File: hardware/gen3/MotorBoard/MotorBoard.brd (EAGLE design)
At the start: 140 x 100 mm, 274 parts, among them M1O1 TEST_PT, M1O2 TEST_PT, M1O3 TEST_PT, M2O1 TEST_PT, M2O2 TEST_PT, M2O3 TEST_PT, M3O1 TEST_PT, M3O2 TEST_PT, M3O3 TEST_PT, M4O1 TEST_PT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

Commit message: resistor values for LEDs
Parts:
- R1, R101, R103, R99: value 130 -> 1k
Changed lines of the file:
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@@
 <attribute name="OC_FARNELL" value="1455104" x="108.225" y="32.425" size="1.778" layer="27" display="off"/>
 </element>
-<element name="R1" library="SparkFun-Passives" package="0805" value="130" x="73" y="91" rot="R270"/>
-<element name="R99" library="SparkFun-Passives" package="0805" value="130" x="67" y="91" rot="R270"/>
-<element name="R101" library="SparkFun-Passives" package="0805" value="130" x="79" y="91" rot="R270"/>
-<element name="R103" library="SparkFun-Passives" package="0805" value="130" x="61" y="91" rot="R270"/>
+<element name="R1" library="SparkFun-Passives" package="0805" value="1k" x="73" y="91" rot="R270"/>
+<element name="R99" library="SparkFun-Passives" package="0805" value="1k" x="67" y="91" rot="R270"/>
+<element name="R101" library="SparkFun-Passives" package="0805" value="1k" x="79" y="91" rot="R270"/>
+<element name="R103" library="SparkFun-Passives" package="0805" value="1k" x="61" y="91" rot="R270"/>
 <element name="LED9" library="SparkFun-LED" package="LED-1206" value="" x="73" y="95.7" rot="R90"/>
 <element name="LED11" library="SparkFun-LED" package="LED-1206" value="" x="67" y="95.7" rot="R90"/>

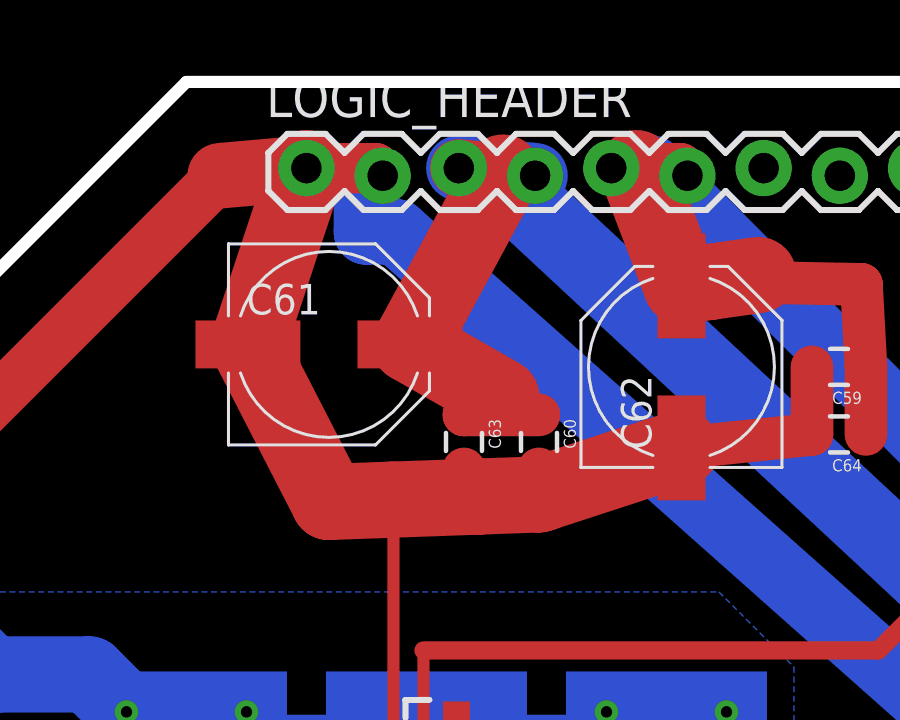
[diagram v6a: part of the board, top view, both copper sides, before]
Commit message: using more pins on logic header
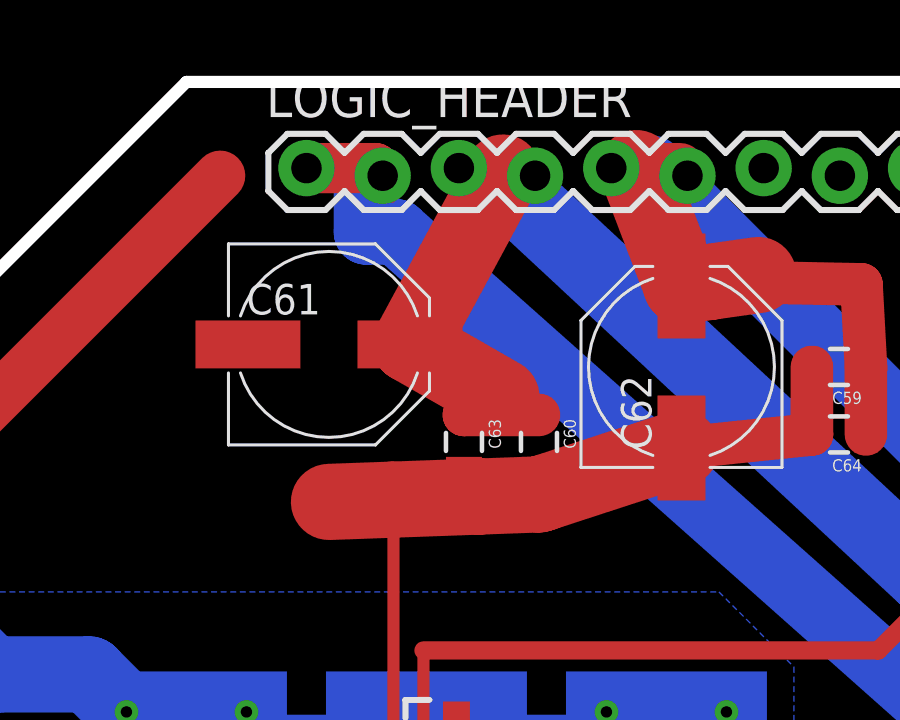
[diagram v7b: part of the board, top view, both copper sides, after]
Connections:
- net 3.3V: now also LOGIC_HEADER.5, LOGIC_HEADER.6, LOGIC_HEADER.7; no longer LOGIC_HEADER.3, LOGIC_HEADER.4
- net 5V: now also LOGIC_HEADER.10, LOGIC_HEADER.8, LOGIC_HEADER.9; no longer LOGIC_HEADER.5, LOGIC_HEADER.6
- net GND: now also LOGIC_HEADER.3, LOGIC_HEADER.4
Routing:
- net GND: track 859.3 -> 842.4 mm
- net 3.3V: track 448.1 -> 442.9 mm
- net 5V: track 654.6 -> 653.4 mm
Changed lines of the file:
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@@
 <via x="65.8" y="59" extent="1-16" drill="0.381"/>
 <via x="44.85" y="77.9" extent="1-16" drill="0.381"/>
-<contactref element="C60" pad="2"/>
-<contactref element="C61" pad="-"/>
 <contactref element="C62" pad="-"/>
 <contactref element="C59" pad="2"/>
-<contactref element="C63" pad="2"/>
 <contactref element="C64" pad="2"/>
-<contactref element="LOGIC_HEADER" pad="1"/>
-<contactref element="LOGIC_HEADER" pad="2"/>
-<wire x1="24" y1="97.127" x2="26.286" y2="97.127" width="1.6764" layer="1"/>
-<wire x1="26.286" y1="97.127" x2="26.54" y2="96.873" width="1.6764" layer="1"/>
-<wire x1="26.85" y1="96.1" x2="26.54" y2="96.873" width="0.254" layer="1"/>
 <contactref element="C46" pad="2"/>
 <contactref element="C45" pad="2"/>
@@
 <via x="89.5" y="24.75" extent="1-16" drill="0.508"/>
 <via x="89.5" y="27" extent="1-16" drill="0.508"/>
-<wire x1="21.123" y1="96.873" x2="24" y2="97.127" width="2.1844" layer="1"/>
-<wire x1="22.05" y1="91.25" x2="24" y2="97.127" width="2.54" layer="1"/>
 <wire x1="36.5" y1="87.8" x2="31.89745625" y2="86.29811875" width="2.54" layer="1"/>
 <wire x1="31.89745625" y1="86.29811875" x2="31.75" y2="86.25" width="2.54" layer="1"/>
@@
 <wire x1="29.77038125" y1="86.1793" x2="26.856240625" y2="86.075221875" width="2.54" layer="1"/>
 <wire x1="26.856240625" y1="86.075221875" x2="24.75" y2="86" width="2.54" layer="1"/>
-<wire x1="24.75" y1="86" x2="22.05" y2="91.25" width="2.54" layer="1"/>
-<wire x1="29.25" y1="87.1" x2="29.77038125" y2="86.1793" width="1.4224" layer="1"/>
-<wire x1="31.75" y1="87.1" x2="31.89745625" y2="86.29811875" width="1.4224" layer="1"/>
 <wire x1="36.5" y1="87.8" x2="40.85" y2="88.25" width="1.4224" layer="1"/>
 <wire x1="40.85" y1="88.25" x2="40.85" y2="90.5" width="1.4224" layer="1"/>
@@
 <wire x1="26.9" y1="84.85" x2="26.9" y2="78" width="0.4064" layer="1"/>
 <wire x1="26.9" y1="84.85" x2="26.856240625" y2="86.075221875" width="0.254" layer="1"/>
-<wire x1="26.55" y1="96.9" x2="26.54" y2="96.873" width="0.254" layer="16"/>
 <wire x1="26.55" y1="96.9" x2="26" y2="96.333" width="0.254" layer="16"/>
 <via x="45.75" y="65.75" extent="1-16" drill="0.508"/>
 <wire x1="45.75" y1="65.75" x2="45.75" y2="63.5" width="1.27" layer="1"/>
+<contactref element="LOGIC_HEADER" pad="1"/>
+<contactref element="LOGIC_HEADER" pad="2"/>
+<contactref element="LOGIC_HEADER" pad="3"/>
+<contactref element="LOGIC_HEADER" pad="4"/>
+<wire x1="24" y1="97.127" x2="26.286" y2="97.127" width="1.6764" layer="1"/>
+<wire x1="26.286" y1="97.127" x2="26.54" y2="96.873" width="1.6764" layer="1"/>
+<wire x1="26.85" y1="96.1" x2="26.54" y2="96.873" width="0.254" layer="1"/>
+<contactref element="C60" pad="2"/>
+<contactref element="C61" pad="-"/>
+<contactref element="C63" pad="2"/>
+<wire x1="29.08" y1="97.127" x2="31.62" y2="96.873" width="0" layer="19" extent="1-1"/>
+<wire x1="26.85" y1="96.1" x2="29.08" y2="97.127" width="0" layer="19" extent="1-1"/>
+<wire x1="26.55" y1="96.9" x2="26.54" y2="96.873" width="0" layer="19" extent="16-16"/>
+<wire x1="21.123" y1="96.873" x2="24" y2="97.127" width="0" layer="19" extent="1-1"/>
+<wire x1="22.05" y1="91.25" x2="26" y2="95" width="0" layer="19" extent="1-16"/>
+<wire x1="24.75" y1="86" x2="22.05" y2="91.25" width="0" layer="19" extent="1-1"/>
+<wire x1="31.75" y1="87.1" x2="31.89745625" y2="86.29811875" width="0" layer="19" extent="1-1"/>
+<wire x1="29.25" y1="87.1" x2="29.77038125" y2="86.1793" width="0" layer="19" extent="1-1"/>
 </signal>
 <signal name="3.3V">
@@
 <contactref element="C61" pad="+"/>
 <contactref element="C63" pad="1"/>
-<contactref element="LOGIC_HEADER" pad="3"/>
-<contactref element="LOGIC_HEADER" pad="4"/>
 <contactref element="C45" pad="1"/>
 <contactref element="C46" pad="1"/>
-<wire x1="31.62" y1="96.873" x2="31.5" y2="95.75" width="1.6764" layer="16"/>
 <wire x1="31.5" y1="95.75" x2="44.71264375" y2="83.459840625" width="2.54" layer="16"/>
 <wire x1="44.71264375" y1="83.459840625" x2="45.10538125" y2="83.094525" width="2.54" layer="16"/>
 <wire x1="45.10538125" y1="83.094525" x2="45.207" y2="83" width="2.54" layer="16"/>
-<wire x1="31.62" y1="96.873" x2="29.08" y2="97.127" width="2.1844" layer="16"/>
 <wire x1="27.45" y1="91.25" x2="30.54801875" y2="96.980196875" width="2.54" layer="1"/>
-<wire x1="30.54801875" y1="96.980196875" x2="29.08" y2="97.127" width="1.9304" layer="1"/>
 <wire x1="27.45" y1="91.25" x2="30.5" y2="89.5" width="2.54" layer="1"/>
 <wire x1="30.5" y1="89.5" x2="29.25" y2="88.9" width="1.4224" layer="1"/>
@@
 <wire x1="110.5" y1="58.9" x2="110.95" y2="58.9" width="0.4064" layer="1"/>
 <wire x1="110.95" y1="58.9" x2="111" y2="58.95" width="0.4064" layer="1"/>
+<contactref element="LOGIC_HEADER" pad="7"/>
+<contactref element="LOGIC_HEADER" pad="6"/>
+<contactref element="LOGIC_HEADER" pad="5"/>
+<wire x1="36.7" y1="96.873" x2="39.24" y2="97.127" width="0" layer="19" extent="1-1"/>
+<wire x1="34.16" y1="97.127" x2="36.7" y2="96.873" width="0" layer="19" extent="1-1"/>
+<wire x1="31.5" y1="95.75" x2="34.16" y2="97.127" width="0" layer="19" extent="16-16"/>
+<wire x1="30.54801875" y1="96.980196875" x2="31.5" y2="95.75" width="0" layer="19" extent="1-16"/>
 </signal>
 <signal name="MOSI">
@@
 </signal>
 <signal name="5V">
-<contactref element="LOGIC_HEADER" pad="5"/>
-<contactref element="LOGIC_HEADER" pad="6"/>
 <contactref element="R93" pad="2"/>
 <contactref element="R62" pad="2"/>
@@
 <wire x1="3.75" y1="42.75" x2="9.627" y2="42.75" width="1.016" layer="1"/>
 <wire x1="9.627" y1="42.75" x2="13.127" y2="40" width="1.016" layer="1"/>
-<wire x1="34.16" y1="97.127" x2="35" y2="97.127" width="1.6764" layer="1"/>
 <wire x1="35" y1="97.127" x2="35.5" y2="97.127" width="1.6764" layer="1"/>
 <wire x1="35.5" y1="97.127" x2="36.446" y2="97.127" width="1.6764" layer="1"/>
-<wire x1="36.446" y1="97.127" x2="36.7" y2="96.873" width="1.6764" layer="1"/>
 <wire x1="13.127" y1="51" x2="13.013965625" y2="53.062425" width="1.4224" layer="1"/>
 <wire x1="13.013965625" y1="53.062425" x2="12.627" y2="60.123" width="1.4224" layer="1"/>
@@
 <wire x1="84.8" y1="38.3" x2="81.2" y2="34.7" width="1.016" layer="1"/>
 <wire x1="81.2" y1="34.7" x2="71.95" y2="34.7" width="0.8128" layer="1"/>
-<wire x1="36.7" y1="96.9" x2="36.7" y2="96.873" width="0.254" layer="16"/>
 <wire x1="36.7" y1="96.9" x2="36.2135" y2="96.4135" width="0.254" layer="16"/>
 <wire x1="33.3" y1="52.3" x2="34.65" y2="50.95" width="0.254" layer="1"/>
@@
 <wire x1="34.65" y1="50.95" x2="34.75" y2="50.725" width="0.254" layer="1"/>
 <wire x1="13.8" y1="53.05" x2="13.7" y2="53.1" width="0.254" layer="1"/>
+<contactref element="LOGIC_HEADER" pad="10"/>
+<contactref element="LOGIC_HEADER" pad="9"/>
+<contactref element="LOGIC_HEADER" pad="8"/>
+<wire x1="44.32" y1="97.127" x2="46.86" y2="96.873" width="0" layer="19" extent="1-1"/>
+<wire x1="41.78" y1="96.873" x2="44.32" y2="97.127" width="0" layer="19" extent="1-1"/>
+<wire x1="42.5" y1="93.25" x2="41.78" y2="96.873" width="0" layer="19" extent="1-1"/>
+<wire x1="35.5" y1="97.127" x2="35.5" y2="97.127" width="0" layer="19" extent="1-16"/>
 </signal>
 <signal name="M1QB">

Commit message: update stuff
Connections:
- net N$110 renamed AVCC
- net N$112 renamed AREF
- net N$12 renamed TDEAD
- net N$8 renamed CP1
- net N$9 renamed CP2
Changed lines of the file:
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@@
 <via x="109.8" y="40.55" extent="1-16" drill="0.381"/>
 </signal>
-<signal name="N$8">
+<signal name="CP1">
 <contactref element="U$4" pad="CP1"/>
 <contactref element="C3" pad="1"/>
@@
 <wire x1="49.625" y1="57.4" x2="49.525" y2="57" width="0.3048" layer="1"/>
 </signal>
-<signal name="N$9">
+<signal name="CP2">
 <contactref element="U$4" pad="CP2"/>
 <contactref element="C3" pad="2"/>
@@
 <wire x1="48.671" y1="57.929" x2="47.725" y2="57" width="0.3048" layer="1"/>
 </signal>
-<signal name="N$12">
+<signal name="TDEAD">
 <contactref element="U$4" pad="TDEAD"/>
 <contactref element="R5" pad="1"/>
@@
 <wire x1="17.95" y1="58.35" x2="15.7" y2="58.35" width="1.27" layer="16"/>
 </signal>
-<signal name="N$110">
+<signal name="AVCC">
 <contactref element="R97" pad="1"/>
 <contactref element="C40" pad="2"/>
@@
 <wire x1="62.75" y1="55.9" x2="62.625" y2="55.85" width="0.254" layer="1"/>
 </signal>
-<signal name="N$112">
+<signal name="AREF">
 <contactref element="U2" pad="62"/>
 <contactref element="C33" pad="2"/>
